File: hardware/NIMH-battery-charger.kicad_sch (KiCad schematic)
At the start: 48 parts, among them J1 USB_A, U1 CH32V003f4u6

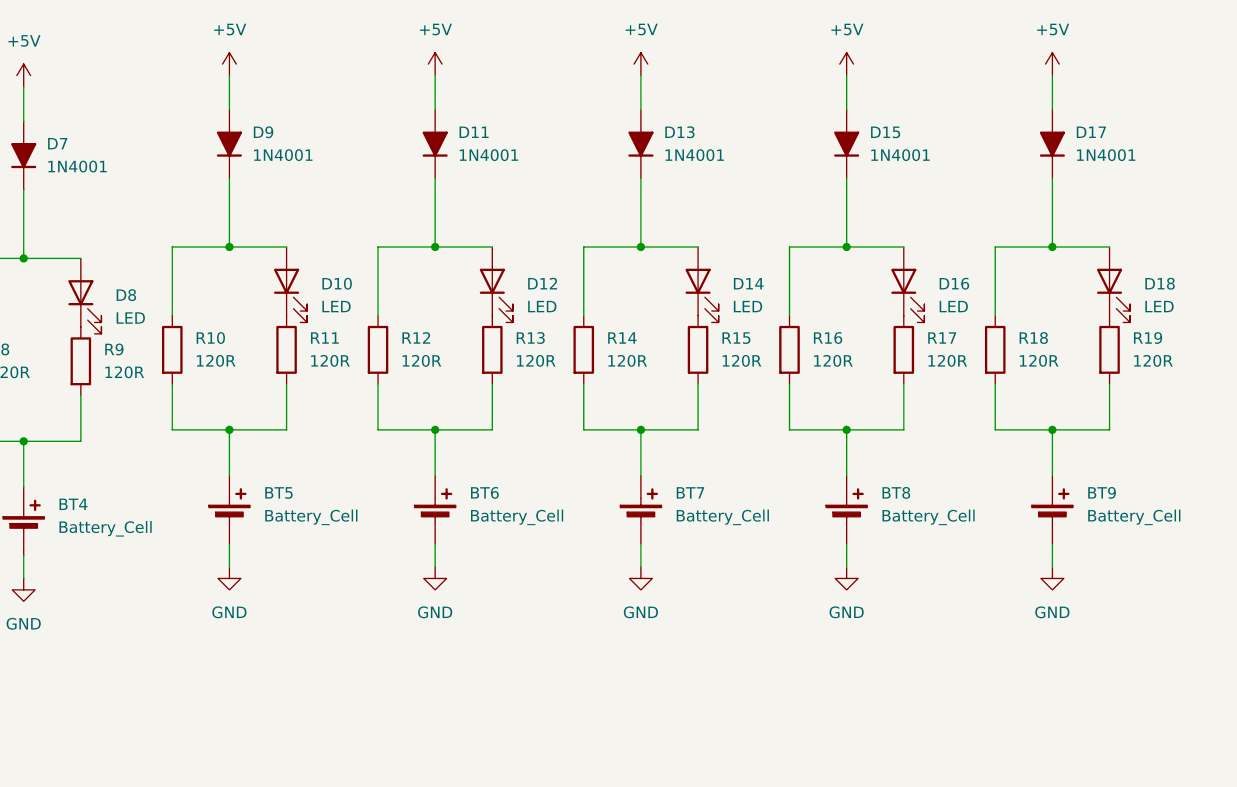
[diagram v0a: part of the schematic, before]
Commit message: Add comments for development board
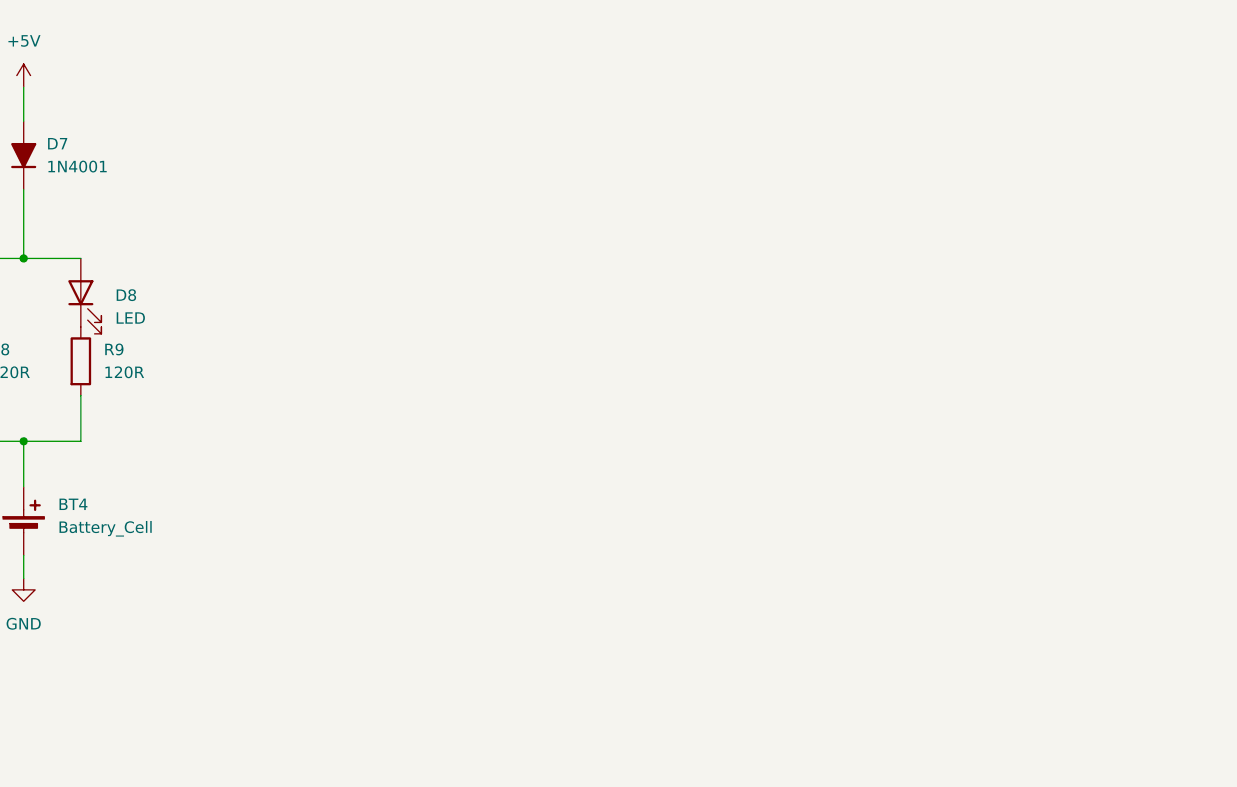
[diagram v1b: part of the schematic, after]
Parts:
- removed BT5, BT6, BT7, BT8, BT9: Battery_Cell, Special_Local:UM-3X1-AA, symbol Device:Battery_Cell
- removed D10, D12, D14, D16, D18: LED, Special_Local:KPTR-3216SGC, symbol Device:LED
- removed D11, D13, D15, D17, D9: 1N4001, PCM_Diode_THT_AKL:D_DO-41_SOD81_P7.62mm_Horizontal, symbol PCM_Diode_AKL:1N4001
- removed R10, R11, R12, R13, R14, R15, R16, R17, R18, R19: 120R, PCM_Resistor_SMD_AKL:R_0603_1608Metric_Pad0.98x0.95mm_HandSolder, symbol Device:R

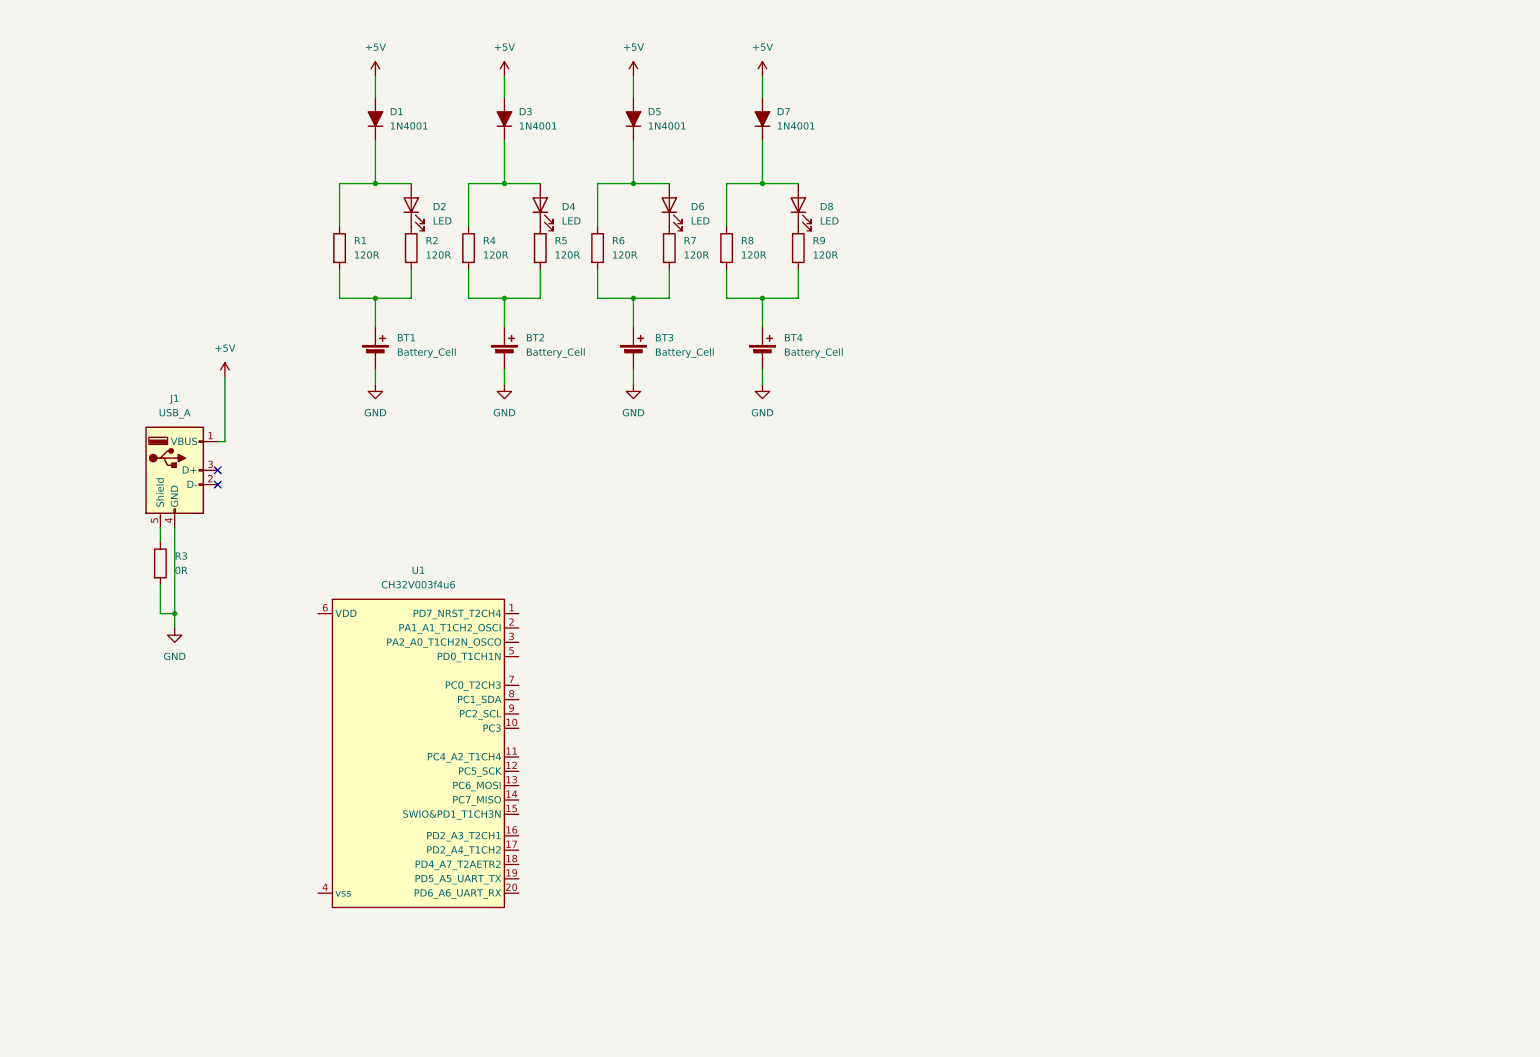
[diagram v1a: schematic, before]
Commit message: Completing schematic and adding comments and images
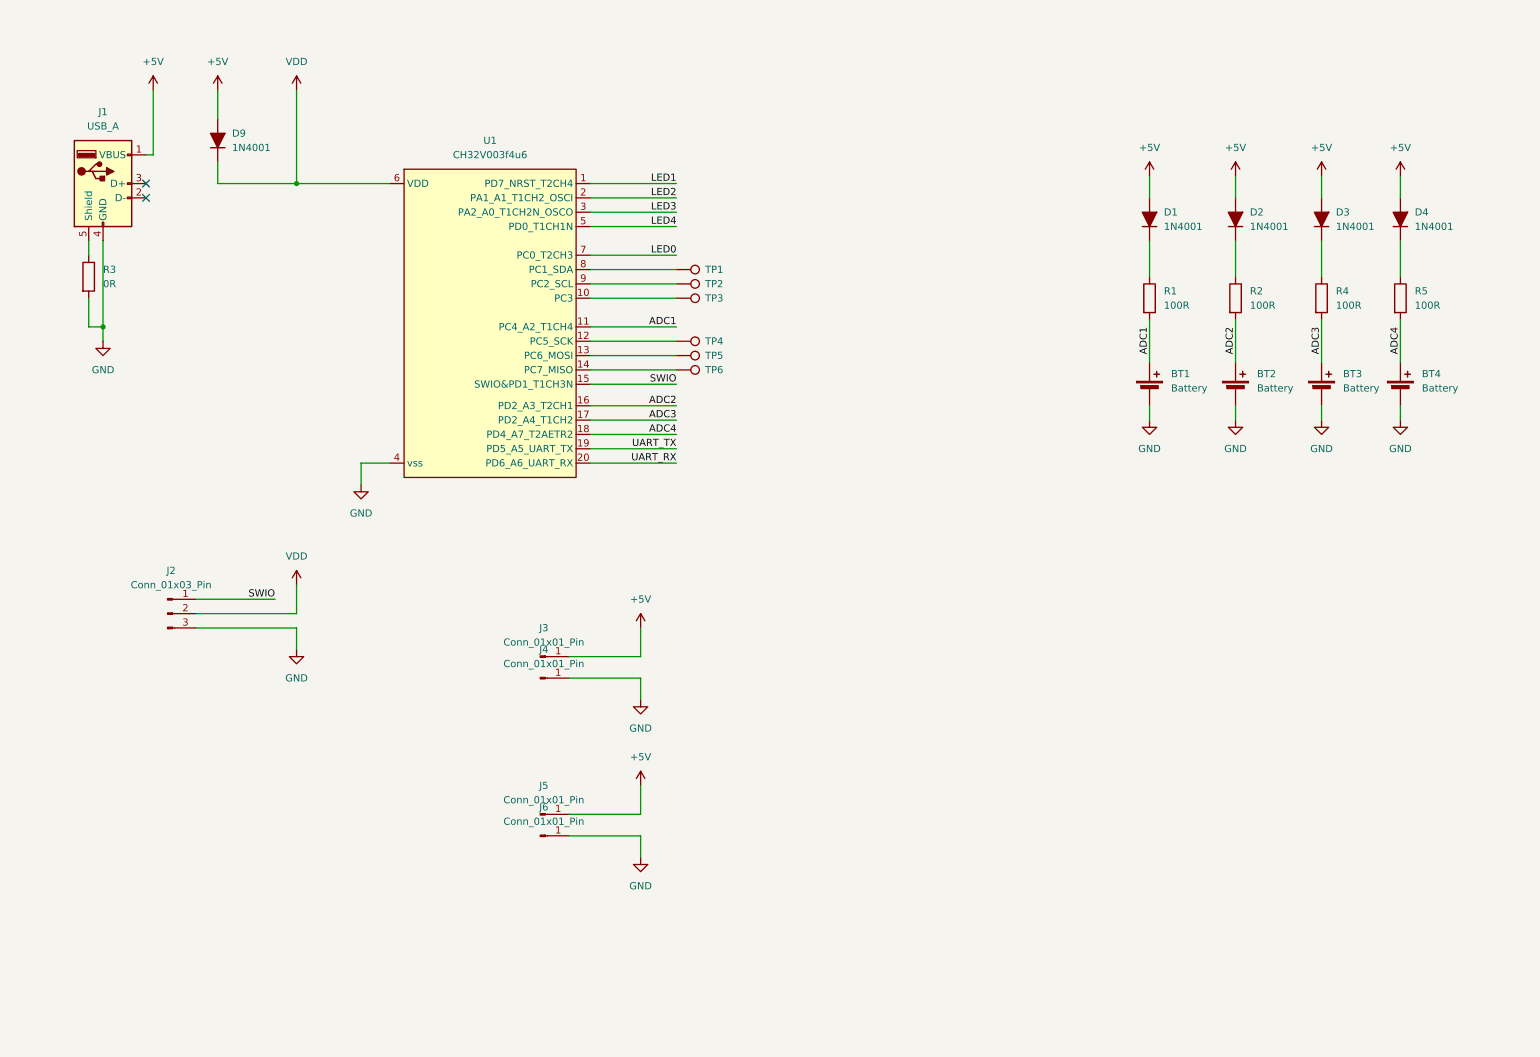
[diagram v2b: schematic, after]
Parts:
- removed D2, D4, D6, D8: LED, Special_Local:KPTR-3216SGC, symbol Device:LED
- removed D5, D7: 1N4001, PCM_Diode_THT_AKL:D_DO-41_SOD81_P7.62mm_Horizontal, symbol PCM_Diode_AKL:1N4001
- removed R6, R7, R8, R9: 120R, PCM_Resistor_SMD_AKL:R_0603_1608Metric_Pad0.98x0.95mm_HandSolder, symbol Device:R
- added D2, D4, D9: 1N4001, PCM_Diode_SMD_Handsoldering_AKL:D_SOD-323_BigPads, symbol PCM_Diode_AKL:1N4001
- added J2: Conn_01x03_Pin, Connector_PinHeader_2.54mm:PinHeader_1x03_P2.54mm_Vertical, symbol Connector:Conn_01x03_Pin
- added J3, J4, J5, J6: Conn_01x01_Pin, Special_Local:PAD, symbol Connector:Conn_01x01_Pin
- added TP1, TP2, TP3, TP4, TP5, TP6: TestPoint, TestPoint:TestPoint_Pad_D1.5mm, symbol Connector:TestPoint
- BT1, BT2, BT3, BT4: value Battery_Cell -> Battery
- D1, D3: footprint PCM_Diode_THT_AKL:D_DO-41_SOD81_P7.62mm_Horizontal -> PCM_Diode_SMD_Handsoldering_AKL:D_SOD-323_BigPads
- J1: footprint Connector_USB:USB_A_Stewart_SS-52100-001_Horizontal -> Connector_USB:USB_A_TE_292303-7_Horizontal
- R1, R2, R4, R5: value 120R -> 100R; footprint PCM_Resistor_SMD_AKL:R_0603_1608Metric_Pad0.98x0.95mm_HandSolder -> PCM_Resistor_SMD_AKL:R_0805_2012Metric_Pad1.20x1.40mm_HandSolder
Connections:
- net +5V: now also D2.2 (A), D4.2 (A), D9.2 (A), J3.1 (Pin_1), J5.1 (Pin_1)
- net GND: now also U1.4 (vss), J2.3 (Pin_3), J4.1 (Pin_1), J6.1 (Pin_1)
- net ADC3: now reaches BT3.1 (+)
- net ADC3: now also R4.2, U1.17 (PD2_A4_T1CH2)
- net ADC1: now reaches BT1.1 (+), R1.2
- net ADC1: now also U1.11 (PC4_A2_T1CH4); no longer R2.2
- net at R5.1: now also D4.1 (K)
- net at R2.1: now also D2.1 (K)
- net ADC4: now reaches BT4.1 (+)
- net ADC4: now also R5.2, U1.18 (PD4_A7_T2AETR2)
- net LED1: now reaches U1.1 (PD7_NRST_T2CH4)
- net at U1.10 (PC3): now also TP3.1
- net at U1.12 (PC5_SCK): now also TP4.1
- net at U1.13 (PC6_MOSI): now also TP5.1
- net at U1.14 (PC7_MISO): now also TP6.1
- net SWIO: now reaches U1.15 (SWIO&PD1_T1CH3N)
- net SWIO: now also J2.1 (Pin_1)
- net ADC2: now reaches U1.16 (PD2_A3_T2CH1)
- net ADC2: now also BT2.1 (+), R2.2
- net UART_TX: now reaches U1.19 (PD5_A5_UART_TX)
- net LED2: now reaches U1.2 (PA1_A1_T1CH2_OSCI)
- net UART_RX: now reaches U1.20 (PD6_A6_UART_RX)
- net LED3: now reaches U1.3 (PA2_A0_T1CH2N_OSCO)
- net LED4: now reaches U1.5 (PD0_T1CH1N)
- net VDD: now reaches U1.6 (VDD)
- net VDD: now also D9.1 (K), J2.2 (Pin_2)
- net LED0: now reaches U1.7 (PC0_T2CH3)
- net at U1.8 (PC1_SDA): now also TP1.1
- net at U1.9 (PC2_SCL): now also TP2.1
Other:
- moved on the sheet: BT1, D1, J1, R1, R3, U1

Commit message: Add USB_C receptacle
Add documents
Resizing the board
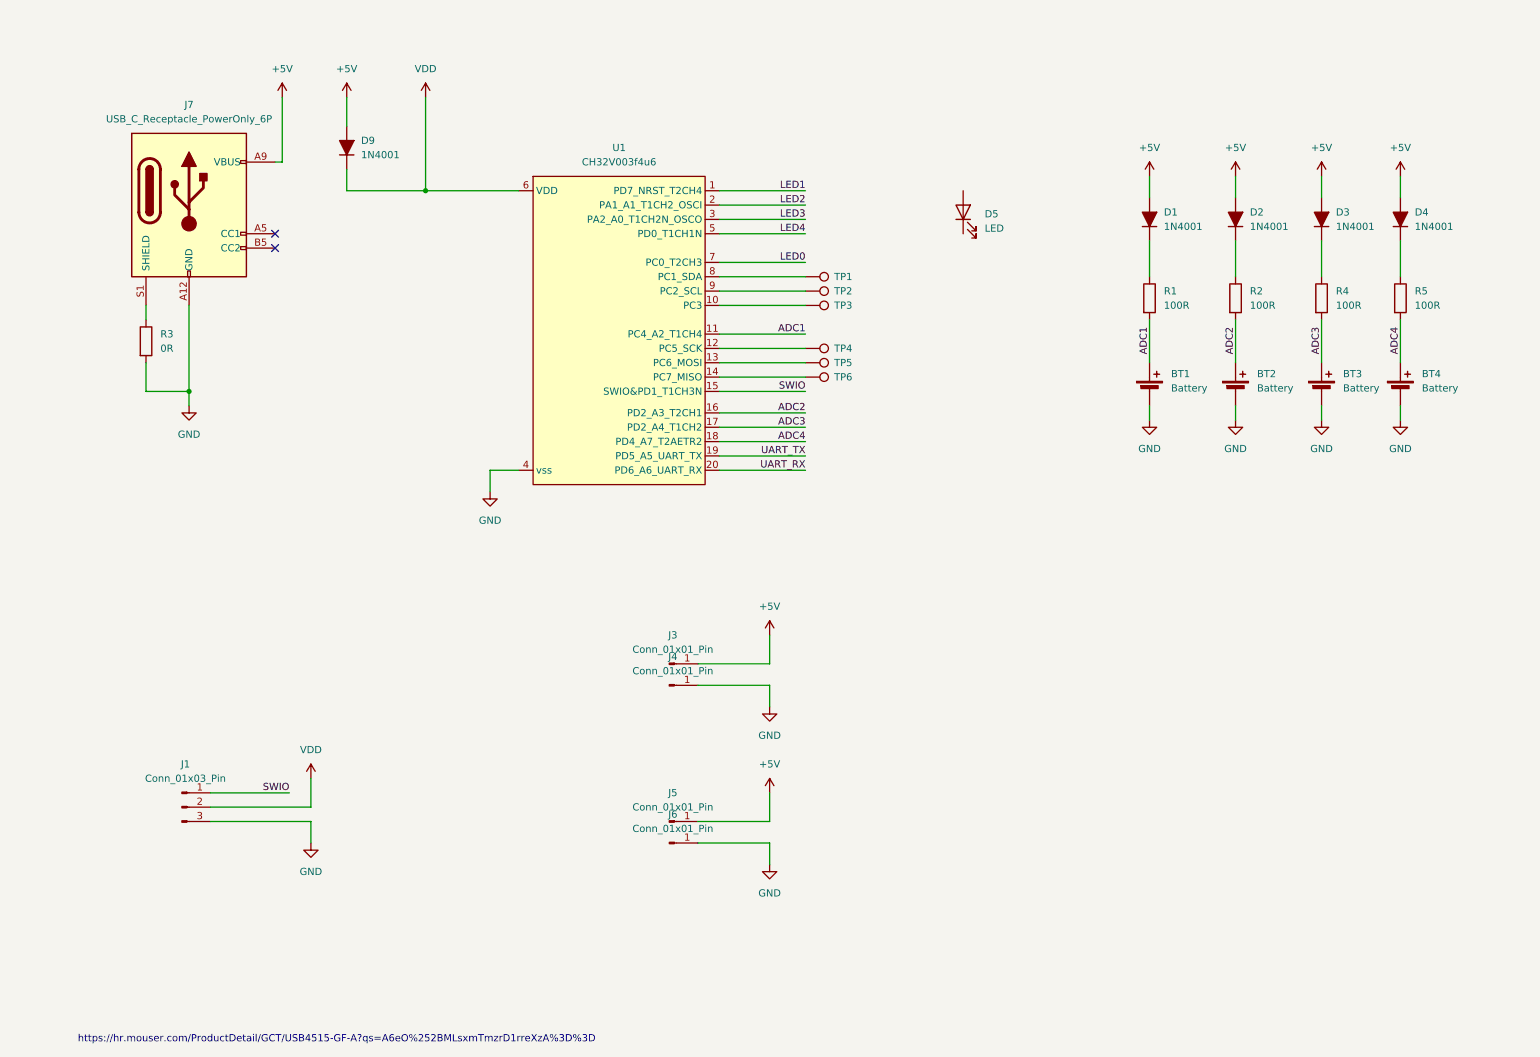
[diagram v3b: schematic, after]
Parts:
- removed J1: USB_A, Connector_USB:USB_A_TE_292303-7_Horizontal, symbol Connector:USB_A
- removed J2: Conn_01x03_Pin, Connector_PinHeader_2.54mm:PinHeader_1x03_P2.54mm_Vertical, symbol Connector:Conn_01x03_Pin
- added D5: LED, symbol Device:LED
- added J1: Conn_01x03_Pin, Connector_Harwin:Harwin_M20-89003xx_1x03_P2.54mm_Horizontal, symbol Connector:Conn_01x03_Pin
- added J7: USB_C_Receptacle_PowerOnly_6P, Special_Local:USB4515-GF-A, symbol Connector:USB_C_Receptacle_PowerOnly_6P
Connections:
- net +5V: now also J7.A9 (VBUS), J7.B9 (VBUS)
- net GND: now also J1.3 (Pin_3), J7.A12 (GND), J7.B12 (GND)
- net SWIO: now also J1.1 (Pin_1)
- net VDD: now also J1.2 (Pin_2)
- net at R3.1: now also J7.S1 (SHIELD)
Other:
- note added: "https://hr.mouser.com/ProductDetail/GCT/USB4515-GF-A?qs=A6eO%252BMLsxmTmzrD1rreXzA%3D%3D"
- moved on the sheet: D9, J3, J4, J5, J6, R3, TP1, TP2, TP3, TP4, TP5, TP6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
